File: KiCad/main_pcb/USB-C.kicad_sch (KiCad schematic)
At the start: 9 parts, among them J2 USB-C, U10 JSMSEMI AMS1117-3.3V, U8 CH340C

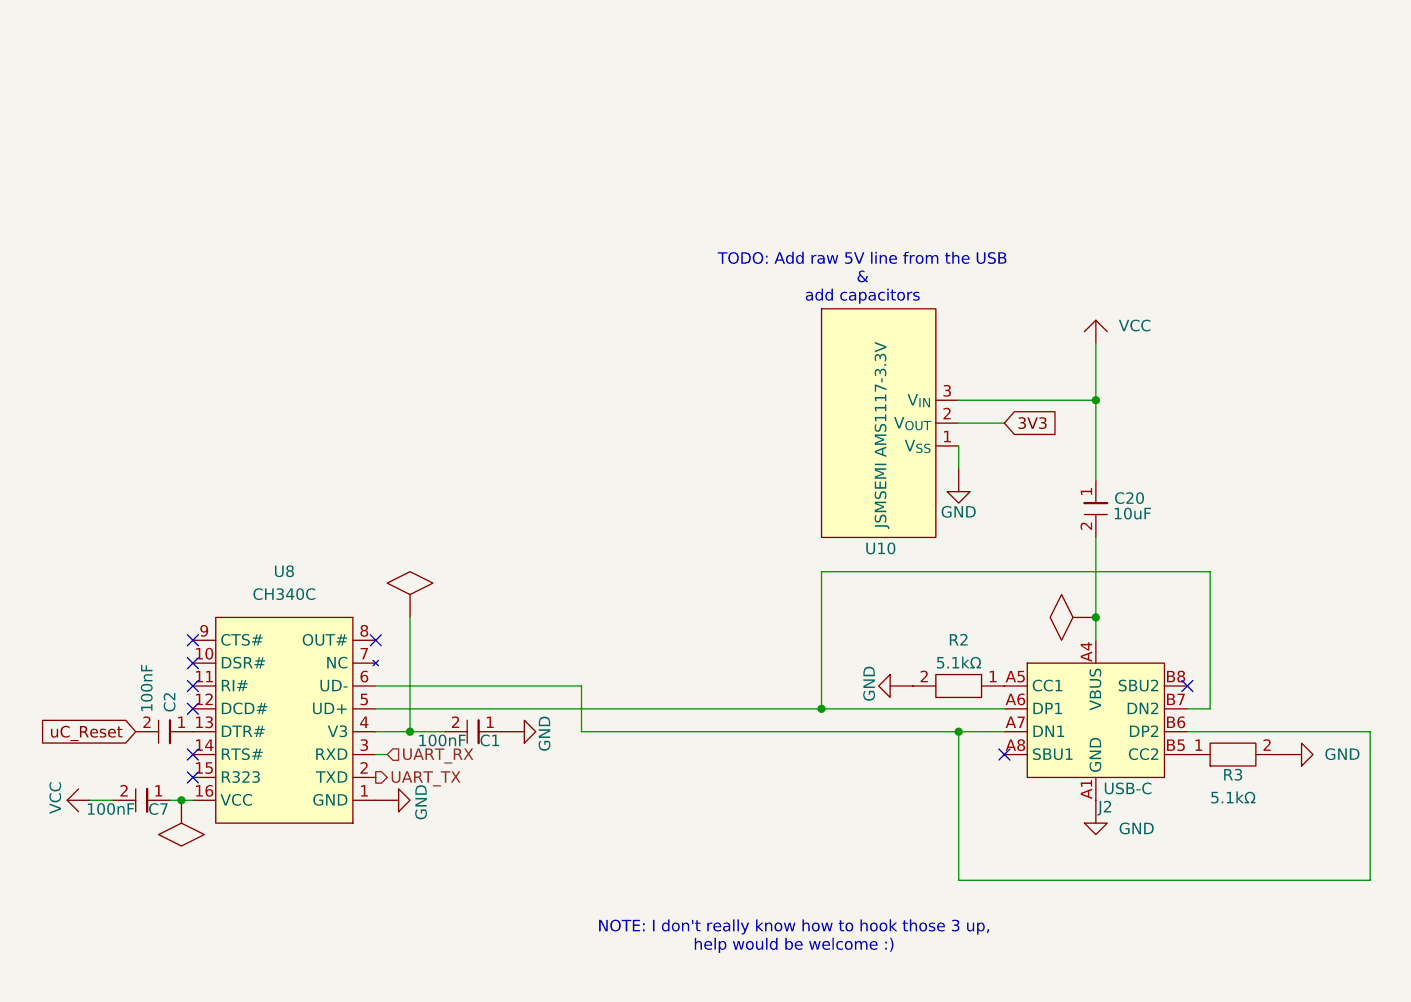
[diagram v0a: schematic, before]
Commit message: feat(KiCad): Adds parallel condensators for USB-C VBUS pin
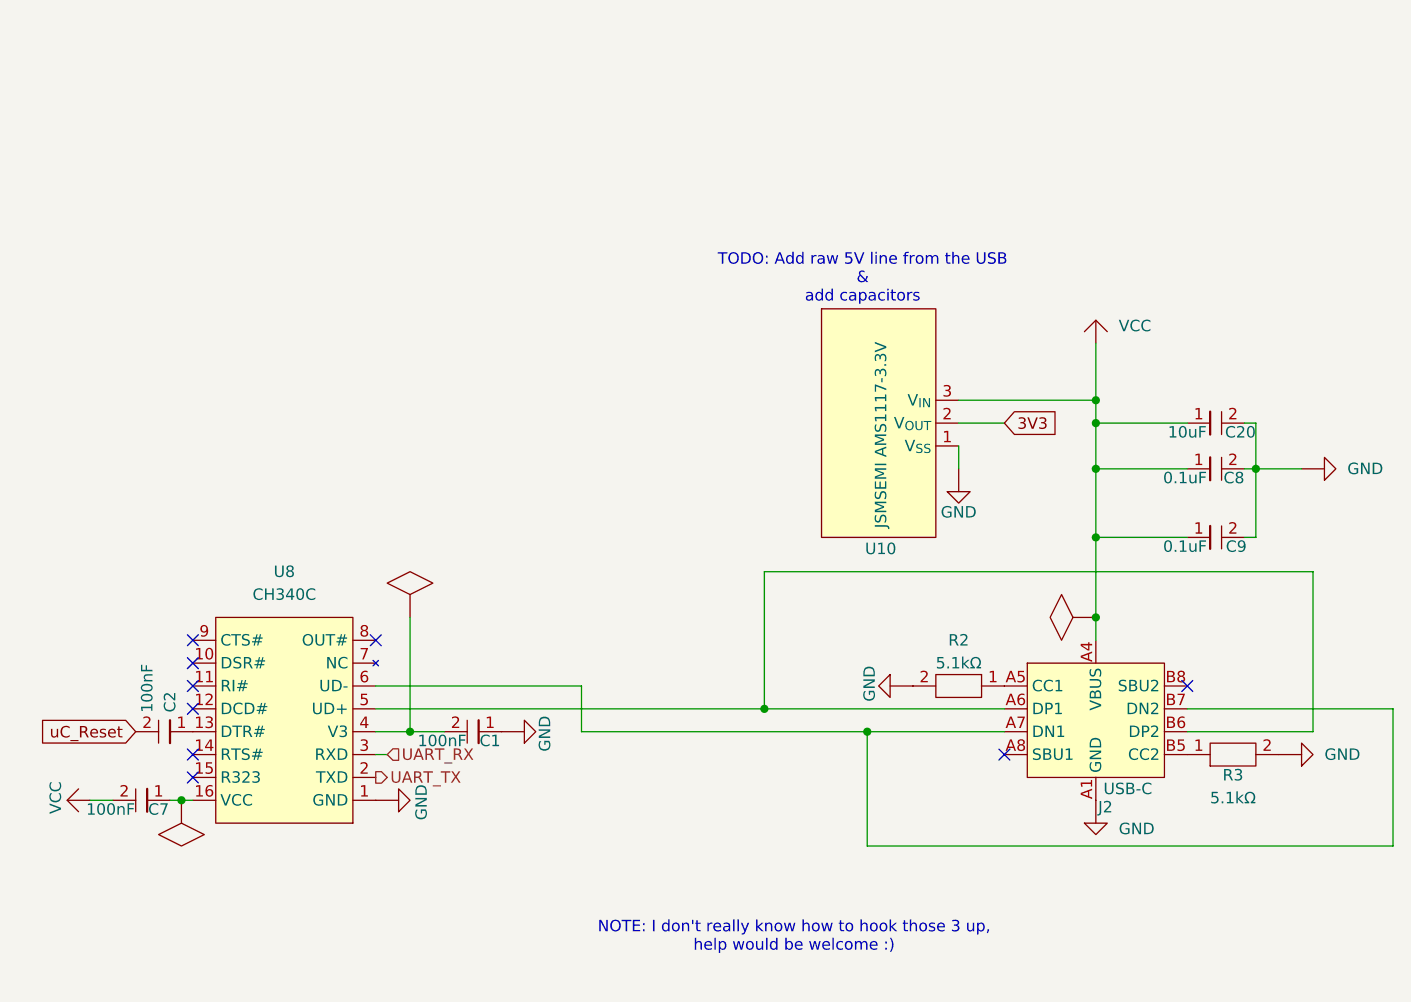
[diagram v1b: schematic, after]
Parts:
- added C8, C9: 0.1uF, symbol lilys_pad:Capacitor
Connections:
- net VCC is gone; now on net VBUS: C20.1, C7.2, U10.3 (V_{IN})
- net GND: now also C20.2, C8.2, C9.2
- net VBUS: now also C8.1, C9.1; no longer C20.2
- net at J2.A6 (DP1), U8.5 (UD+): now also J2.B6 (DP2); no longer J2.B7 (DN2)
- net at J2.A7 (DN1), U8.6 (UD-): now also J2.B7 (DN2); no longer J2.B6 (DP2)
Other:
- moved on the sheet: C20

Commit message: feat(KiCad): Fixes symbols and ERC
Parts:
- C1, C2, C20, C7, C8, C9: symbol lilys_pad:Capacitor -> Lily's Pad:Capacitor
- J2: symbol lilys_pad:USB_TYPE-C-31-M-14 -> Lily's Pad:USB_TYPE-C-31-M-14
- R2, R3: symbol lilys_pad:Resistor -> Lily's Pad:Resistor
- U10: symbol lilys_pad:JSMSEMI_AMS1117-3.3V -> Lily's Pad:JSMSEMI_AMS1117-3.3V
- U8: footprint (none) -> lilys_pad:CH340C; symbol lilys_pad:CH340C -> Lily's Pad:CH340C

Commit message: feat(KiCad): Continues work
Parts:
- added J5, J6: 1x1 Header, symbol Lily's Pad:1x1_Heaer
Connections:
- net VBUS: now also J2.A6 (DP1), J2.B6 (DP2), U8.5 (UD+), J5.1, J6.1
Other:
- moved on the sheet: C20, C8, C9, U10

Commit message: feat(KiCad): Continues work
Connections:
- net GND: now also C7.2
- net VBUS: now also C7.1, U8.16 (VCC); no longer C7.2
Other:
- moved on the sheet: C7
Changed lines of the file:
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@@
-	)
-	(junction
-		(at 92.71 107.95)
-		(diameter 0)
-		(color 0 0 0 0)
 	)
 	(junction
@@
 	)
 	(junction
+		(at 62.23 115.57)
+		(diameter 0)
+		(color 0 0 0 0)
+	)
+	(junction
 		(at 168.91 90.17)
 		(diameter 0)
@@
 	)
 	(junction
-		(at 67.31 115.57)
-		(diameter 0)
-		(color 0 0 0 0)
-	)
-	(junction
 		(at 186.69 53.34)
 		(diameter 0)
@@
 	(wire
 		(pts
+			(xy 57.15 115.57) (xy 62.23 115.57)
+		)
+		(stroke
+			(width 0)
+			(type default)
+		)
+	)
+	(wire
+		(pts
 			(xy 186.69 48.26) (xy 186.69 53.34)
 		)
@@
 	(wire
 		(pts
-			(xy 92.71 107.95) (xy 88.9 107.95)
+			(xy 105.41 107.95) (xy 102.87 107.95)
 		)
 		(stroke
@@
 	(wire
 		(pts
+			(xy 62.23 128.27) (xy 62.23 124.46)
+		)
+		(stroke
+			(width 0)
+			(type default)
+		)
+	)
+	(wire
+		(pts
+			(xy 62.23 115.57) (xy 62.23 118.11)
+		)
+		(stroke
+			(width 0)
+			(type default)
+		)
+	)
+	(wire
+		(pts
 			(xy 132.08 105.41) (xy 158.75 105.41)
 		)
@@
 	(wire
 		(pts
-			(xy 57.15 115.57) (xy 59.69 115.57)
+			(xy 62.23 115.57) (xy 68.58 115.57)
 		)
 		(stroke
@@
 	(wire
 		(pts
-			(xy 96.52 107.95) (xy 92.71 107.95)
-		)
-		(stroke
-			(width 0)
-			(type default)
-		)
-	)
-	(wire
-		(pts
-			(xy 92.71 95.25) (xy 92.71 107.95)
+			(xy 88.9 107.95) (xy 96.52 107.95)
 		)
 		(stroke
@@
 	(wire
 		(pts
-			(xy 67.31 115.57) (xy 68.58 115.57)
-		)
-		(stroke
-			(width 0)
-			(type default)
-		)
-	)
-	(wire
-		(pts
 			(xy 179.07 107.95) (xy 193.04 107.95)
 		)
@@
 		(pts
 			(xy 132.08 90.17) (xy 132.08 105.41)
-		)
-		(stroke
-			(width 0)
-			(type default)
-		)
-	)
-	(wire
-		(pts
-			(xy 66.04 115.57) (xy 67.31 115.57)
 		)
 		(stroke
@@
 	(symbol
 		(lib_id "Lily's Pad:GND")
-		(at 105.41 107.95 90)
+		(at 107.95 107.95 90)
 		(unit 1)
 		(exclude_from_sim no)
@@
 		(dnp no)
 		(property "Reference" "#PWR012"
+			(at 110.49 107.95 0)
+			(effects
+				(font
+					(size 1.27 1.27)
+				)
+				(hide yes)
+			)
+		)
+		(property "Value" "GND"
+			(at 110.236 106.172 0)
+			(effects
+				(font
+					(size 1.27 1.27)
+				)
+				(justify right)
+			)
+		)
+		(property "Footprint" ""
 			(at 107.95 107.95 0)
 			(effects
@@
 			)
 		)
-		(property "Value" "GND"
-			(at 107.696 106.172 0)
-			(effects
-				(font
-					(size 1.27 1.27)
-				)
-				(justify right)
-			)
-		)
-		(property "Footprint" ""
-			(at 105.41 107.95 0)
-			(effects
-				(font
-					(size 1.27 1.27)
-				)
-				(hide yes)
-			)
-		)
 		(property "Datasheet" ""
-			(at 105.41 107.95 0)
-			(effects
-				(font
-					(size 1.27 1.27)
-				)
-				(hide yes)
-			)
-		)
-		(property "Description" ""
-			(at 105.41 107.95 0)
+			(at 107.95 107.95 0)
+			(effects
+				(font
+					(size 1.27 1.27)
+				)
+				(hide yes)
+			)
+		)
+		(property "Description" ""
+			(at 107.95 107.95 0)
 			(effects
 				(font
@@
 	(symbol
 		(lib_id "Lily's Pad:Capacitor")
-		(at 62.23 115.57 270)
+		(at 62.23 121.92 0)
 		(unit 1)
 		(exclude_from_sim no)
@@
 		(dnp no)
 		(property "Reference" "C7"
-			(at 64.77 116.586 90)
+			(at 63.246 119.38 90)
 			(effects
 				(font
@@
 		)
 		(property "Value" "100nF"
-			(at 59.436 116.586 90)
+			(at 63.246 124.714 90)
 			(effects
 				(font
@@
 		)
 		(property "Footprint" ""
-			(at 62.23 115.57 0)
+			(at 62.23 121.92 0)
 			(effects
 				(font
@@
 		)
 		(property "Datasheet" ""
-			(at 62.23 115.57 0)
-			(effects
-				(font
-					(size 1.27 1.27)
-				)
-				(hide yes)
-			)
-		)
-		(property "Description" ""
-			(at 62.23 115.57 0)
+			(at 62.23 121.92 0)
+			(effects
+				(font
+					(size 1.27 1.27)
+				)
+				(hide yes)
+			)
+		)
+		(property "Description" ""
+			(at 62.23 121.92 0)
 			(effects
 				(font
@@
 				(path "/346fb29b-2426-4b69-9f9a-e979b6e41832/a4816677-4d4e-4f2e-882a-ab61f6eb2b02"
 					(reference "C9")
-					(unit 1)
-				)
-			)
-		)
-	)
-	(symbol
-		(lib_id "Lily's Pad:PWR_FLG")
-		(at 92.71 92.71 180)
-		(unit 1)
-		(exclude_from_sim no)
-		(in_bom no)
-		(on_board no)
-		(dnp no)
-		(fields_autoplaced yes)
-		(property "Reference" "#PWR027"
-			(at 92.71 92.71 0)
-			(effects
-				(font
-					(size 1.27 1.27)
-				)
-				(hide yes)
-			)
-		)
-		(property "Value" "PWR_FLG"
-			(at 92.71 92.71 0)
-			(effects
-				(font
-					(size 1.27 1.27)
-				)
-				(hide yes)
-			)
-		)
-		(property "Footprint" ""
-			(at 92.71 92.71 0)
-			(effects
-				(font
-					(size 1.27 1.27)
-				)
-				(hide yes)
-			)
-		)
-		(property "Datasheet" ""
-			(at 92.71 92.71 0)
-			(effects
-				(font
-					(size 1.27 1.27)
-				)
-				(hide yes)
-			)
-		)
-		(property "Description" ""
-			(at 92.71 92.71 0)
-			(effects
-				(font
-					(size 1.27 1.27)
-				)
-				(hide yes)
-			)
-		)
-		(pin "1"
-		)
-		(instances
-			(project "main_pcb"
-				(path "/346fb29b-2426-4b69-9f9a-e979b6e41832/a4816677-4d4e-4f2e-882a-ab61f6eb2b02"
-					(reference "#PWR027")
 					(unit 1)
 				)
@@
 	)
 	(symbol
+		(lib_id "Lily's Pad:GND")
+		(at 62.23 130.81 0)
+		(unit 1)
+		(exclude_from_sim no)
+		(in_bom no)
+		(on_board no)
+		(dnp no)
+		(fields_autoplaced yes)
+		(property "Reference" "#PWR018"
+			(at 62.23 133.35 0)
+			(effects
+				(font
+					(size 1.27 1.27)
+				)
+				(hide yes)
+			)
+		)
+		(property "Value" "GND"
+			(at 62.23 134.62 0)
+			(effects
+				(font
+					(size 1.27 1.27)
+				)
+			)
+		)
+		(property "Footprint" ""
+			(at 62.23 130.81 0)
+			(effects
+				(font
+					(size 1.27 1.27)
+				)
+				(hide yes)
+			)
+		)
+		(property "Datasheet" ""
+			(at 62.23 130.81 0)
+			(effects
+				(font
+					(size 1.27 1.27)
+				)
+				(hide yes)
+			)
+		)
+		(property "Description" ""
+			(at 62.23 130.81 0)
+			(effects
+				(font
+					(size 1.27 1.27)
+				)
+				(hide yes)
+			)
+		)
+		(pin "1"
+		)
+		(instances
+			(project "main_pcb"
+				(path "/346fb29b-2426-4b69-9f9a-e979b6e41832/a4816677-4d4e-4f2e-882a-ab61f6eb2b02"
+					(reference "#PWR018")
+					(unit 1)
+				)
+			)
+		)
+	)
+	(symbol
 		(lib_id "Lily's Pad:JSMSEMI_AMS1117-3.3V")
 		(at 144.78 48.26 0)
@@
 					(unit 1)
 				)
-			)
-		)
-	)
-	(symbol
-		(lib_id "Lily's Pad:PWR_FLG")
-		(at 67.31 118.11 0)
-		(unit 1)
-		(exclude_from_sim no)
-		(in_bom no)
-		(on_board no)
-		(dnp no)
-		(fields_autoplaced yes)
-		(property "Reference" "#PWR041"
-			(at 67.31 118.11 0)
-			(effects
-				(font
-					(size 1.27 1.27)
-				)
-				(hide yes)
-			)
-		)
-		(property "Value" "PWR_FLG"
-			(at 67.31 118.11 0)
-			(effects
-				(font
-					(size 1.27 1.27)
-				)
-				(hide yes)
-			)
-		)
-		(property "Footprint" ""
-			(at 67.31 118.11 0)
-			(effects
-				(font
-					(size 1.27 1.27)
-				)
-				(hide yes)
-			)
-		)
-		(property "Datasheet" ""
-			(at 67.31 118.11 0)
-			(effects
-				(font
-					(size 1.27 1.27)
-				)
-				(hide yes)
-			)
-		)
-		(property "Description" ""
-			(at 67.31 118.11 0)
-			(effects
-				(font
-					(size 1.27 1.27)
-				)
-				(hide yes)
-			)
-		)
-		(pin "1"
-		)
-		(instances
-			(project "main_pcb"
-				(path "/346fb29b-2426-4b69-9f9a-e979b6e41832/a4816677-4d4e-4f2e-882a-ab61f6eb2b02"
-					(reference "#PWR041")
-					(unit 1)
-				)

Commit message: feat(KiCad): Continues work
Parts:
- C1, C2, C20, C7, C8, C9: footprint (none) -> Capacitor_SMD:C_0201_0603Metric_Pad0.64x0.40mm_HandSolder
- J5, J6: footprint (none) -> Connector_JST:JST_XH_B1B-XH-AM_1x01_P2.50mm_Vertical
- R2, R3: footprint (none) -> Resistor_SMD:R_0201_0603Metric_Pad0.64x0.40mm_HandSolder
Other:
- note removed: "NOTE: I don't really know how to hook those 3 up, help would be welcome :)"
- note removed: "TODO: Add raw 5V line from the USB & add capacitors"
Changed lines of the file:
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@@
 	(generator_version "9.0")
 	(paper "A4")
-	(text "TODO: Add raw 5V line from the USB\n&\nadd capacitors"
-		(exclude_from_sim no)
-		(at 143.002 32.258 0)
-		(effects
-			(font
-				(size 1.27 1.27)
-			)
-		)
-	)
-	(text "NOTE: I don't really know how to hook those 3 up,\nhelp would be welcome :)\n"
-		(exclude_from_sim no)
-		(at 135.382 130.81 0)
-		(effects
-			(font
-				(size 1.27 1.27)
-			)
-		)
-	)
 	(junction
 		(at 143.51 107.95)
@@
 			)
 		)
-		(property "Footprint" ""
+		(property "Footprint" "Capacitor_SMD:C_0201_0603Metric_Pad0.64x0.40mm_HandSolder"
 			(at 182.88 48.26 0)
 			(effects
@@
 			)
 		)
-		(property "Footprint" ""
+		(property "Footprint" "Capacitor_SMD:C_0201_0603Metric_Pad0.64x0.40mm_HandSolder"
 			(at 64.77 107.95 0)
 			(effects
@@
 			)
 		)
-		(property "Footprint" ""
+		(property "Footprint" "Resistor_SMD:R_0201_0603Metric_Pad0.64x0.40mm_HandSolder"
 			(at 184.15 110.49 0)
 			(effects
@@
 			)
 		)
-		(property "Footprint" ""
+		(property "Footprint" "Capacitor_SMD:C_0201_0603Metric_Pad0.64x0.40mm_HandSolder"
 			(at 99.06 107.95 0)
 			(effects
@@
 			)
 		)
-		(property "Footprint" ""
+		(property "Footprint" "Capacitor_SMD:C_0201_0603Metric_Pad0.64x0.40mm_HandSolder"
 			(at 62.23 121.92 0)
 			(effects
@@
 			)
 		)
-		(property "Footprint" ""
+		(property "Footprint" "Capacitor_SMD:C_0201_0603Metric_Pad0.64x0.40mm_HandSolder"
 			(at 182.88 60.96 0)
 			(effects
@@
 			)
 		)
-		(property "Footprint" ""
+		(property "Footprint" "Connector_JST:JST_XH_B1B-XH-AM_1x01_P2.50mm_Vertical"
 			(at 168.91 72.39 0)
 			(effects
@@
 			)
 		)
-		(property "Footprint" ""
+		(property "Footprint" "Connector_JST:JST_XH_B1B-XH-AM_1x01_P2.50mm_Vertical"
 			(at 168.91 78.74 0)
 			(effects
@@
 			)
 		)
-		(property "Footprint" ""
+		(property "Footprint" "Capacitor_SMD:C_0201_0603Metric_Pad0.64x0.40mm_HandSolder"
 			(at 182.88 53.34 0)
 			(effects
@@
 			)
 		)
-		(property "Footprint" ""
+		(property "Footprint" "Resistor_SMD:R_0201_0603Metric_Pad0.64x0.40mm_HandSolder"
 			(at 153.67 102.87 0)
 			(effects

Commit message: feat(KiCad): Continues work
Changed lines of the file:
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@@
 		(dnp no)
 		(property "Reference" "R3"
-			(at 184.15 112.776 90)
+			(at 184.15 110.49 90)
 			(effects
 				(font
@@
 		)
 		(property "Value" "5.1kΩ"
-			(at 184.15 115.316 90)
+			(at 184.15 113.03 90)
 			(effects
 				(font
@@
 		(dnp no)
 		(property "Reference" "R2"
-			(at 153.67 97.79 90)
-			(effects
-				(font
+			(at 153.67 102.87 90)
+			(effects
+				(font
